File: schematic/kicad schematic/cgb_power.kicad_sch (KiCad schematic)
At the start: 26 parts, among them Q3 2SC4081, U5 DC-DC

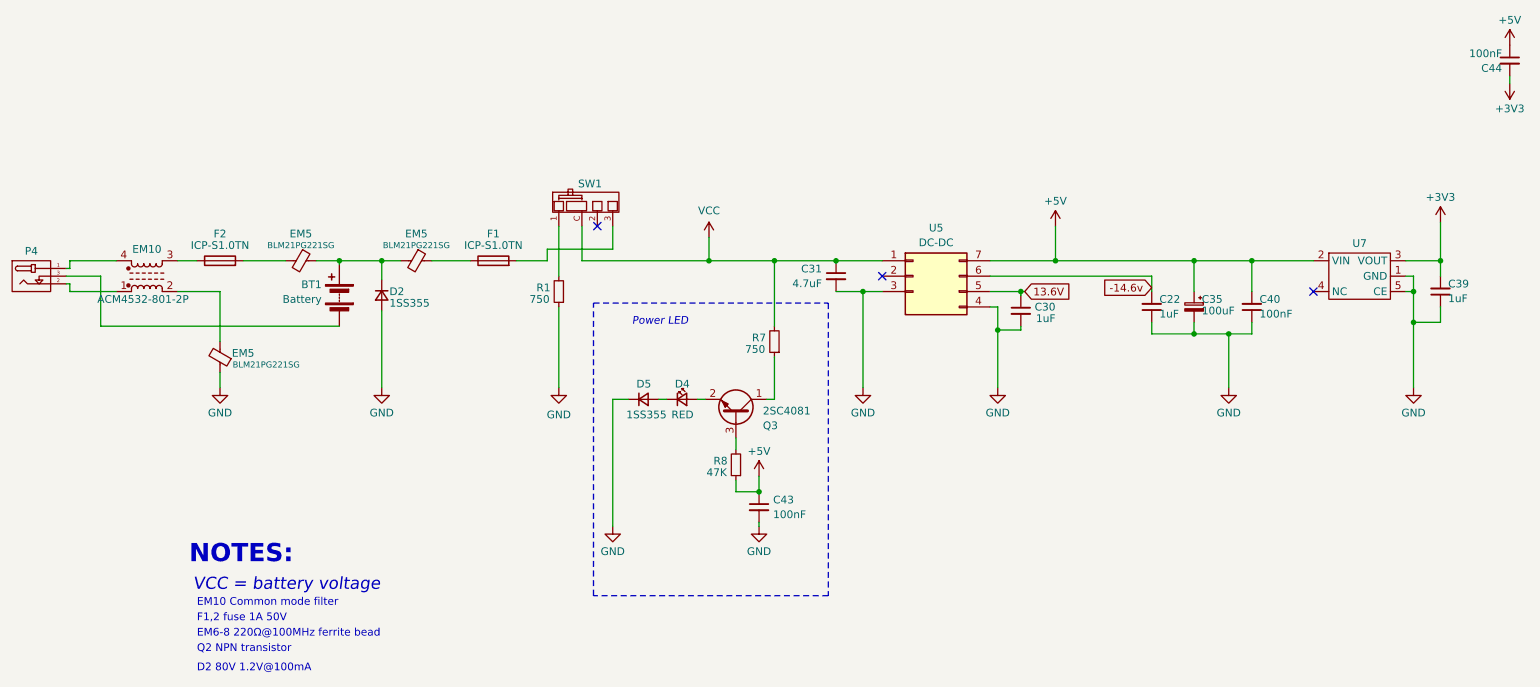
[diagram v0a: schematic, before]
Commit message: fixed schematic, thx giltesa and darren
the ir transistor was labelled wrong
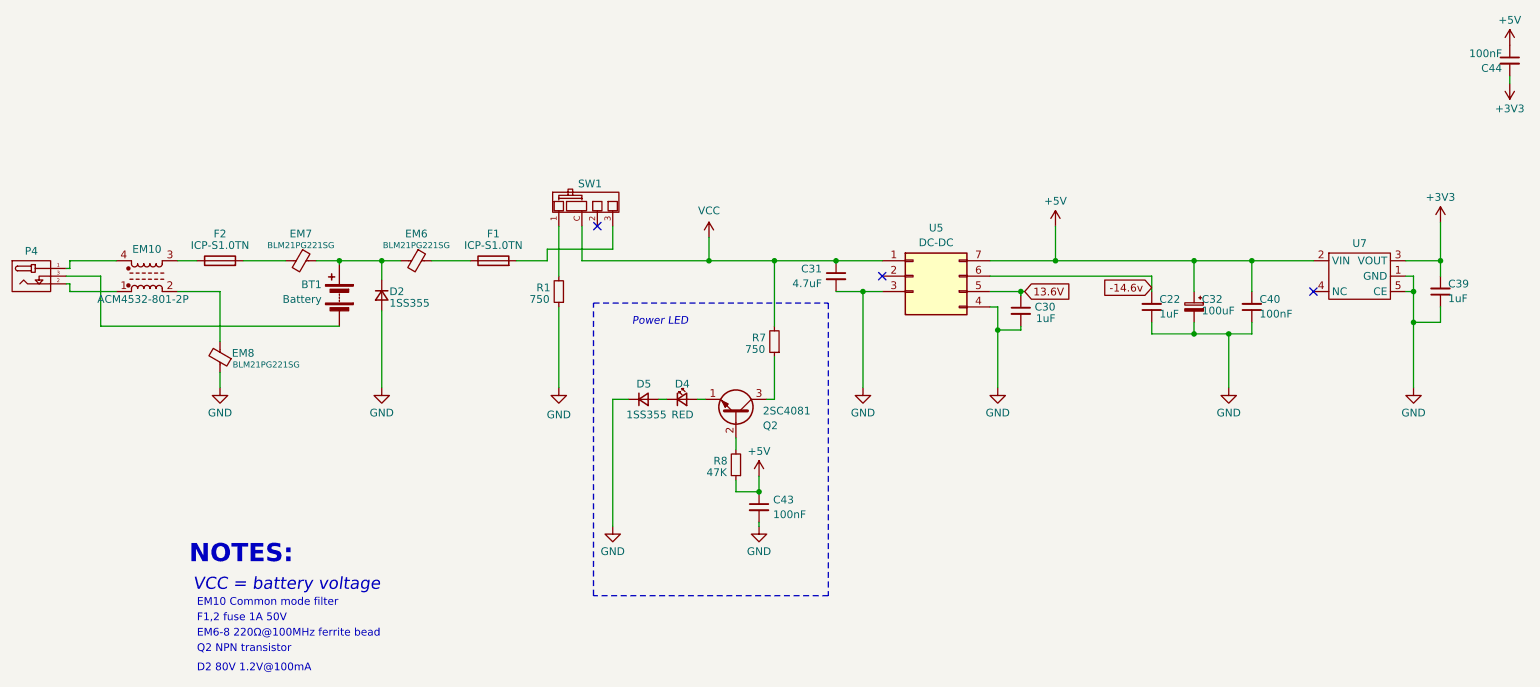
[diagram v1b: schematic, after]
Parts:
- renumbered C35 to C32, EM5 to EM6, EM5 to EM7, EM5 to EM8, Q3 to Q2
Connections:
- net at R8.2: now also Q2.2; no longer Q2.3 (C)
- net at R7.1: now also Q2.3 (E); no longer Q2.1 (E)
- net at D4.2 (A): now also Q2.1 (B); no longer Q2.2 (B)
